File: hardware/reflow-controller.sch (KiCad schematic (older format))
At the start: 20 parts, among them J1 USB_B_Mini, J2 Conn_01x02, J3 Conn_02x03_Odd_Even, J4 Conn_01x02, J5 Conn_01x04, Q1 BC817, U1 MAX31855KASA, U2 AP2127K-3.3, U3 ATMEGA8U2-AU, Y1 8MHz

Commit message: PCB passes DRC.
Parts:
- removed J1: USB_B_Mini, symbol Connector_Specialized:USB_B_Mini
- removed U3: ATMEGA8U2-AU, TQFP-32, symbol MCU_Atmel_ATMEGA:ATMEGA8U2-AU
- added C7, C8: 0.1u, Capacitor_SMD:C_0603_1608Metric, symbol Device:C
- added C9: 10n, Capacitor_SMD:C_0603_1608Metric, symbol Device:C
- added D2: LED, LED_SMD:LED_0603_1608Metric, symbol Device:LED
- added J1: USB_B_Mini, Connector_USB:USB_Mini-B_Lumberg_2486_01_Horizontal, symbol Connector:USB_B_Mini
- added R4: 240, Resistor_SMD:R_0603_1608Metric, symbol Device:R
- added R5: 10k, Resistor_SMD:R_0603_1608Metric, symbol Device:R
- added R6: 1k, Resistor_SMD:R_0603_1608Metric, symbol Device:R
- added U3: ATmega8U2-AU, Package_QFP:TQFP-32_7x7mm_P0.8mm, symbol MCU_Microchip_ATmega:ATmega8U2-AU
- C1, C2, C3, C4, C5, C6: footprint (none) -> Capacitor_SMD:C_0603_1608Metric
- D1: footprint (none) -> Diode_SMD:D_SOD-323
- J2: footprint (none) -> TerminalBlock_Phoenix:TerminalBlock_Phoenix_MKDS-1,5-2_1x02_P5.00mm_Horizontal
- J3: footprint (none) -> Connector_PinHeader_2.54mm:PinHeader_2x03_P2.54mm_Vertical
- J4: footprint (none) -> Connector_PinHeader_2.54mm:PinHeader_1x02_P2.54mm_Vertical
- J5: footprint (none) -> Connector_PinHeader_2.54mm:PinHeader_1x04_P2.54mm_Vertical
- R1, R2: footprint (none) -> Resistor_SMD:R_0603_1608Metric
- R3: value 4.7k -> 10k; footprint (none) -> Resistor_SMD:R_0603_1608Metric
- Y1: footprint (none) -> Crystal:Crystal_SMD_HC49-SD
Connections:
- wire segments 78 -> 100
- no-connect marks 16 -> 15
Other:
- moved on the sheet: C1, C4, C5, C6, D1, J2, J4, Q1, R1, R2, R3, Y1

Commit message: Fixed power supply when programmed by ISP, added mounting holes, replaced mini USB connector with micro connector.
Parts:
- removed J1: USB_B_Mini, Connector_USB:USB_Mini-B_Lumberg_2486_01_Horizontal, symbol Connector:USB_B_Mini
- added J1: USB_B_Micro, Connector_USB:USB_Micro-B_Amphenol_10103594-0001LF_Horizontal, symbol Connector:USB_B_Micro
- added MH1, MH2, MH3, MH4: MountingHole_Pad, MountingHole:MountingHole_2.7mm_M2.5_Pad_Via, symbol Mechanical:MountingHole_Pad
- U3: symbol MCU_Microchip_ATmega:ATmega8U2-AU -> reflow-controller-rescue:ATmega8U2-AU-MCU_Microchip_ATmega
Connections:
- wire segments 100 -> 104
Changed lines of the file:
@@
 	7950 1550 8300 1550
 Text Label 8300 1550 2    50   ~ 0
-VCC
+VBUS
 Wire Wire Line
 	7950 1650 8300 1650
@@
 	5500 3800 5500 3950
 $Comp
-L MCU_Microchip_ATmega:ATmega8U2-AU U3
+L reflow-controller-rescue:ATmega8U2-AU-MCU_Microchip_ATmega U3
 U 1 1 5B3659A5
 P 7400 4400
@@
 Wire Wire Line
 	7300 2700 7300 2400
-$Comp
-L Connector:USB_B_Mini J1
-U 1 1 5B3FB3D2
-P 2500 4350
-F 0 "J1" H 2555 4817 50  0000 C CNN
-F 1 "USB_B_Mini" H 2555 4726 50  0000 C CNN
-F 2 "Connector_USB:USB_Mini-B_Lumberg_2486_01_Horizontal" H 2650 4300 50  0001 C CNN
-F 3 "~" H 2650 4300 50  0001 C CNN
-	1    2500 4350
-	1    0    0    -1
-$EndComp
 NoConn ~ 2800 4550
 Wire Wire Line
@@
 Wire Wire Line
 	2550 1700 2550 1800
+$Comp
+L Connector:USB_B_Micro J1
+U 1 1 5BB4219C
+P 2500 4350
+F 0 "J1" H 2555 4817 50  0000 C CNN
+F 1 "USB_B_Micro" H 2555 4726 50  0000 C CNN
+F 2 "Connector_USB:USB_Micro-B_Amphenol_10103594-0001LF_Horizontal" H 2650 4300 50  0001 C CNN
+F 3 "~" H 2650 4300 50  0001 C CNN
+	1    2500 4350
+	1    0    0    -1
+$EndComp
+$Comp
+L Mechanical:MountingHole_Pad MH2
+U 1 1 5BB44E9C
+P 1600 1250
+F 0 "MH2" H 1700 1301 50  0000 L CNN
+F 1 "MountingHole_Pad" H 1700 1210 50  0000 L CNN
+F 2 "MountingHole:MountingHole_2.7mm_M2.5_Pad_Via" H 1600 1250 50  0001 C CNN
+F 3 "~" H 1600 1250 50  0001 C CNN
+	1    1600 1250
+	1    0    0    -1
+$EndComp
+$Comp
+L Mechanical:MountingHole_Pad MH3
+U 1 1 5BB44F1A
+P 10600 1100
+F 0 "MH3" H 10700 1151 50  0000 L CNN
+F 1 "MountingHole_Pad" H 10700 1060 50  0000 L CNN
+F 2 "MountingHole:MountingHole_2.7mm_M2.5_Pad_Via" H 10600 1100 50  0001 C CNN
+F 3 "~" H 10600 1100 50  0001 C CNN
+	1    10600 1100
+	1    0    0    -1
+$EndComp
+$Comp
+L Mechanical:MountingHole_Pad MH4
+U 1 1 5BB44F98
+P 10600 6050
+F 0 "MH4" H 10700 6101 50  0000 L CNN
+F 1 "MountingHole_Pad" H 10700 6010 50  0000 L CNN
+F 2 "MountingHole:MountingHole_2.7mm_M2.5_Pad_Via" H 10600 6050 50  0001 C CNN
+F 3 "~" H 10600 6050 50  0001 C CNN
+	1    10600 6050
+	1    0    0    -1
+$EndComp
+$Comp
+L Mechanical:MountingHole_Pad MH1
+U 1 1 5BB4500A
+P 1500 6150
+F 0 "MH1" H 1600 6201 50  0000 L CNN
+F 1 "MountingHole_Pad" H 1600 6110 50  0000 L CNN
+F 2 "MountingHole:MountingHole_2.7mm_M2.5_Pad_Via" H 1500 6150 50  0001 C CNN
+F 3 "~" H 1500 6150 50  0001 C CNN
+	1    1500 6150
+	1    0    0    -1
+$EndComp
+$Comp
+L power:GND #PWR0101
+U 1 1 5BB451EE
+P 1600 1500
+F 0 "#PWR0101" H 1600 1250 50  0001 C CNN
+F 1 "GND" H 1605 1327 50  0000 C CNN
+F 2 "" H 1600 1500 50  0001 C CNN
+F 3 "" H 1600 1500 50  0001 C CNN
+	1    1600 1500
+	1    0    0    -1
+$EndComp
+$Comp
+L power:GND #PWR0102
+U 1 1 5BB45237
+P 1500 6400
+F 0 "#PWR0102" H 1500 6150 50  0001 C CNN
+F 1 "GND" H 1505 6227 50  0000 C CNN
+F 2 "" H 1500 6400 50  0001 C CNN
+F 3 "" H 1500 6400 50  0001 C CNN
+	1    1500 6400
+	1    0    0    -1
+$EndComp
+$Comp
+L power:GND #PWR0113
+U 1 1 5BB45280
+P 10600 6300
+F 0 "#PWR0113" H 10600 6050 50  0001 C CNN
+F 1 "GND" H 10605 6127 50  0000 C CNN
+F 2 "" H 10600 6300 50  0001 C CNN
+F 3 "" H 10600 6300 50  0001 C CNN
+	1    10600 6300
+	1    0    0    -1
+$EndComp
+$Comp
+L power:GND #PWR0114
+U 1 1 5BB4FB0F
+P 10600 1350
+F 0 "#PWR0114" H 10600 1100 50  0001 C CNN
+F 1 "GND" H 10605 1177 50  0000 C CNN
+F 2 "" H 10600 1350 50  0001 C CNN
+F 3 "" H 10600 1350 50  0001 C CNN
+	1    10600 1350
+	1    0    0    -1
+$EndComp
+Wire Wire Line
+	10600 1350 10600 1200
+Wire Wire Line
+	10600 6150 10600 6300
+Wire Wire Line
+	1500 6250 1500 6400
+Wire Wire Line
+	1600 1500 1600 1350
 $EndSCHEMATC

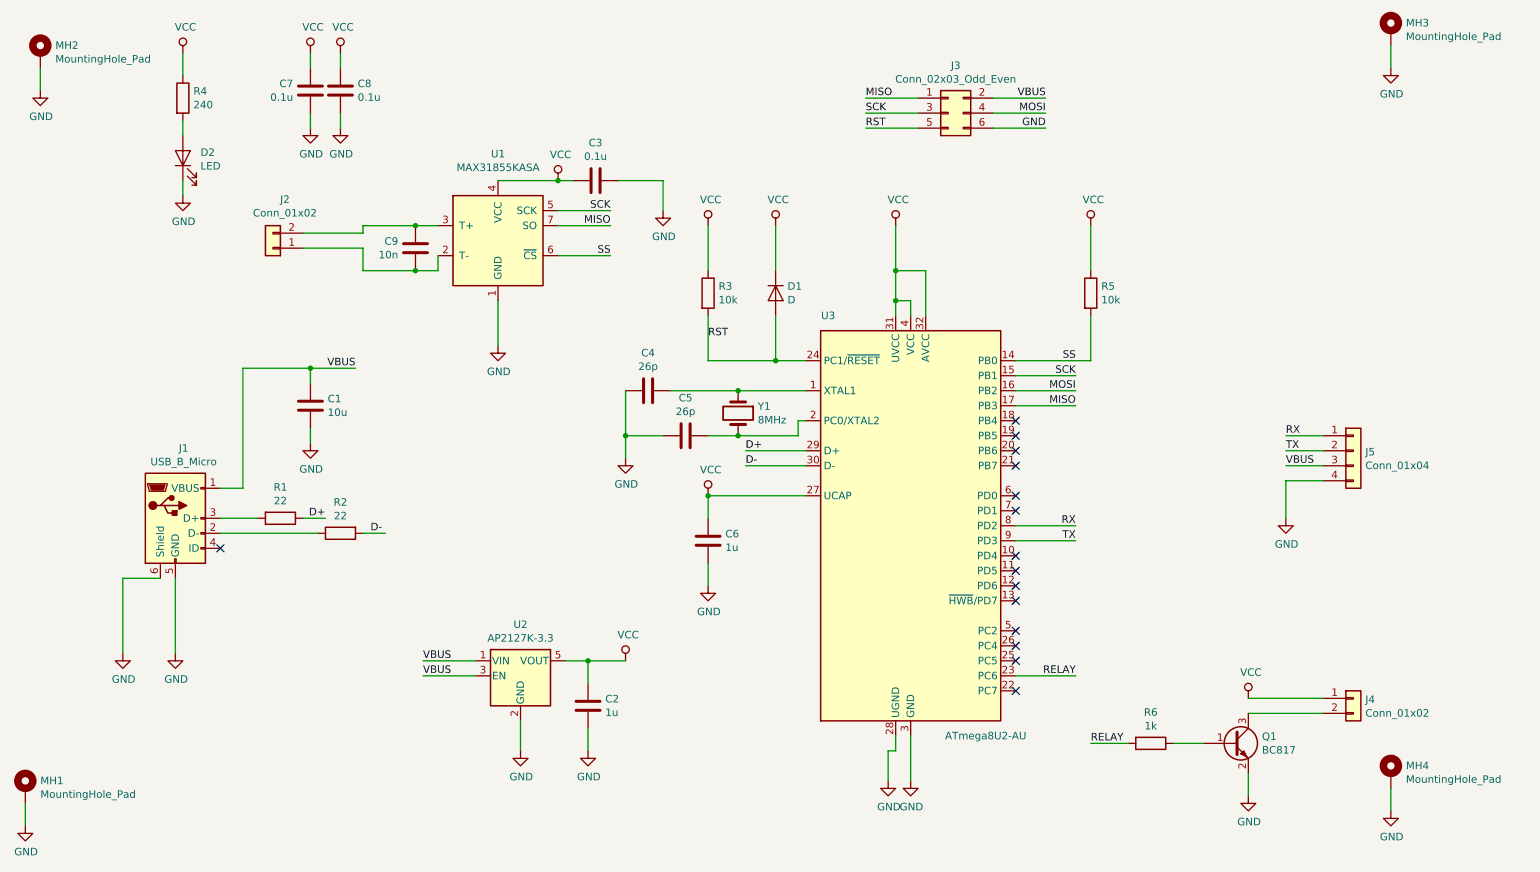
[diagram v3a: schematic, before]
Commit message: Bom generation improvements.
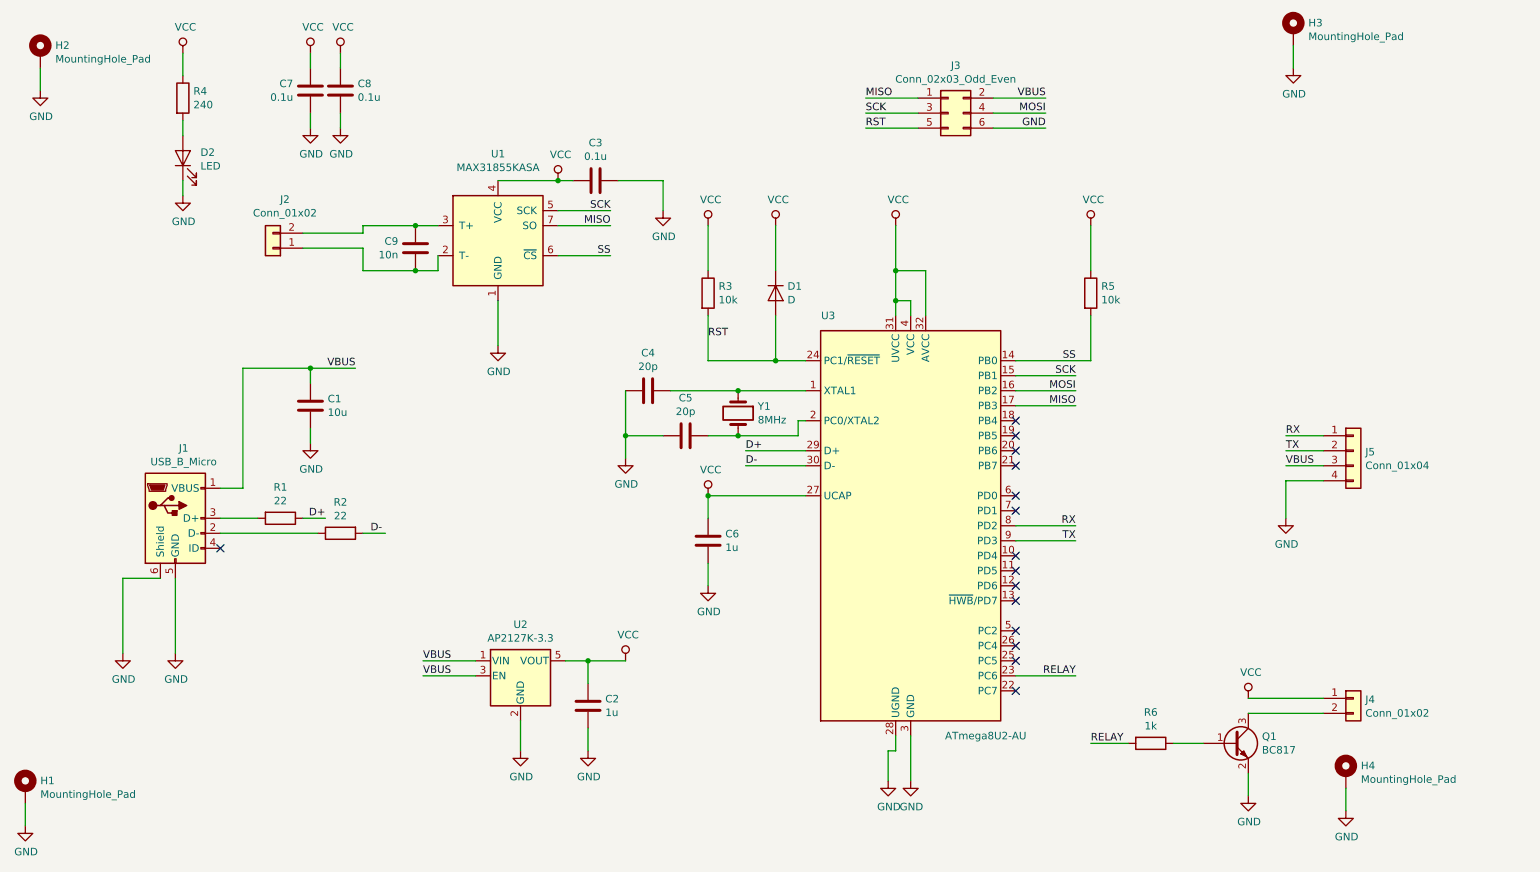
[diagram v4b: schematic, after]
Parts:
- C1: MFN (none) -> CL10A106KP8NNNC
- C2, C6: MFN (none) -> GRM188R60J105KA01D
- C3, C7, C8: MFN (none) -> CL10B104KO8NNNC
- C4, C5: value 26p -> 20p; MFN (none) -> CL10C200JB8NNNC
- C9: MFN (none) -> C1608X7R2A103M080AA
- D1: MFN (none) -> 1N4148WS-7-F
- D2: MFN (none) -> SML-D12V8WT86
- J2: MFN (none) -> 1935161
- Q1: MFN (none) -> BC817-40Q-13-F; manf# BC817-40Q-13-F -> (none)
- R1, R2: MFN (none) -> CR0603-JW-220ELF; Tolerance 5% -> (none)
- R3, R5: MFN (none) -> CR0603-FX-1002HLF
- R4: MFN (none) -> ERA-3AEB241V
- R6: MFN (none) -> CR0603-FX-1001HLF
- U1: MFN (none) -> MAX31855KASA+T; manf# MAX31855KASA+T -> (none)
- U2: MFN (none) -> AP2127K-3.3TRG1; manf# AP2127K-3.3TRG1 -> (none)
- U3: MFN (none) -> ATMEGA8U2-AU
- Y1: MFN (none) -> ABLS-8.000MHZ-B4-T; manf# ABLS-8.000MHZ-B4-T -> (none)
- renumbered MH1 to H1, MH2 to H2, MH3 to H3, MH4 to H4
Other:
- moved on the sheet: H3, H4
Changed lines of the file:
@@
 EESchema Schematic File Version 4
 LIBS:reflow-controller-cache
-EELAYER 29 0
+EELAYER 26 0
 EELAYER END
 $Descr A4 11693 8268
@@
 F 2 "Resistor_SMD:R_0603_1608Metric" V 3130 4350 50  0001 C CNN
 F 3 "~" H 3200 4350 50  0001 C CNN
-F 4 "5%" V 3200 4350 50  0001 C CNN "Tolerance"
+F 4 "CR0603-JW-220ELF" V 3200 4350 50  0001 C CNN "MFN"
 	1    3200 4350
 	0    1    1    0
@@
 F 2 "Resistor_SMD:R_0603_1608Metric" V 3530 4450 50  0001 C CNN
 F 3 "~" H 3600 4450 50  0001 C CNN
-F 4 "5%" V 3600 4450 50  0001 C CNN "Tolerance"
+F 4 "CR0603-JW-220ELF" V 3600 4450 50  0001 C CNN "MFN"
 	1    3600 4450
 	0    -1   1    0
@@
 F 2 "Capacitor_SMD:C_0603_1608Metric" H 6088 4350 50  0001 C CNN
 F 3 "~" H 6050 4500 50  0001 C CNN
+F 4 "GRM188R60J105KA01D" H 6050 4500 50  0001 C CNN "MFN"
 	1    6050 4500
 	1    0    0    -1
@@
 F 2 "Crystal:Crystal_SMD_HC49-SD" H 6250 3650 50  0001 C CNN
 F 3 "~" H 6250 3650 50  0001 C CNN
-F 4 "ABLS-8.000MHZ-B4-T" V 6250 3650 50  0001 C CNN "manf#"
+F 4 "ABLS-8.000MHZ-B4-T" V 6250 3650 50  0001 C CNN "MFN"
 	1    6250 3650
 	0    1    1    0
@@
 P 5650 3500
 F 0 "C4" V 5398 3500 50  0000 C CNN
-F 1 "26p" V 5489 3500 50  0000 C CNN
+F 1 "20p" V 5489 3500 50  0000 C CNN
 F 2 "Capacitor_SMD:C_0603_1608Metric" H 5688 3350 50  0001 C CNN
 F 3 "~" H 5650 3500 50  0001 C CNN
+F 4 "CL10C200JB8NNNC" V 5650 3500 50  0001 C CNN "MFN"
 	1    5650 3500
 	0    1    1    0
@@
 P 5900 3800
 F 0 "C5" V 5648 3800 50  0000 C CNN
-F 1 "26p" V 5739 3800 50  0000 C CNN
+F 1 "20p" V 5739 3800 50  0000 C CNN
 F 2 "Capacitor_SMD:C_0603_1608Metric" H 5938 3650 50  0001 C CNN
 F 3 "~" H 5900 3800 50  0001 C CNN
+F 4 "CL10C200JB8NNNC" V 5900 3800 50  0001 C CNN "MFN"
 	1    5900 3800
 	0    1    1    0
@@
 F 2 "Package_SO:SOIC-8_3.9x4.9mm_P1.27mm" H 5650 2150 50  0001 C CIN
 F 3 "http://datasheets.maximintegrated.com/en/ds/MAX31855.pdf" H 4650 2500 50  0001 C CNN
-F 4 "MAX31855KASA+T" H 4650 2500 50  0001 C CNN "manf#"
+F 4 "MAX31855KASA+T" H 4650 2500 50  0001 C CNN "MFN"
 	1    4650 2500
 	1    0    0    -1
@@
 F 2 "Capacitor_SMD:C_0603_1608Metric" H 5338 1950 50  0001 C CNN
 F 3 "~" H 5300 2100 50  0001 C CNN
+F 4 "CL10B104KO8NNNC" V 5300 2100 50  0001 C CNN "MFN"
 	1    5300 2100
 	0    1    1    0
@@
 F 2 "TerminalBlock_Phoenix:TerminalBlock_Phoenix_MKDS-1,5-2_1x02_P5.00mm_Horizontal" H 3150 2550 50  0001 C CNN
 F 3 "~" H 3150 2550 50  0001 C CNN
+F 4 "1935161" H 3150 2550 50  0001 C CNN "MFN"
 	1    3150 2550
 	-1   0    0    1
@@
 F 2 "Resistor_SMD:R_0603_1608Metric" V 5980 2850 50  0001 C CNN
 F 3 "~" H 6050 2850 50  0001 C CNN
+F 4 "CR0603-FX-1002HLF" H 6050 2850 50  0001 C CNN "MFN"
 	1    6050 2850
 	1    0    0    -1
@@
 F 2 "Diode_SMD:D_SOD-323" H 6500 2850 50  0001 C CNN
 F 3 "~" H 6500 2850 50  0001 C CNN
+F 4 "1N4148WS-7-F" V 6500 2850 50  0001 C CNN "MFN"
 	1    6500 2850
 	0    1    1    0
@@
 F 2 "Package_TO_SOT_SMD:SOT-23-5" H 4800 5725 50  0001 C CNN
 F 3 "https://www.diodes.com/assets/Datasheets/AP2127.pdf" H 4800 5500 50  0001 C CNN
-F 4 "AP2127K-3.3TRG1" H 4800 5400 50  0001 C CNN "manf#"
+F 4 "AP2127K-3.3TRG1" H 4800 5400 50  0001 C CNN "MFN"
 	1    4800 5400
 	1    0    0    -1
@@
 F 2 "Capacitor_SMD:C_0603_1608Metric" H 3438 3450 50  0001 C CNN
 F 3 "~" H 3400 3600 50  0001 C CNN
+F 4 "CL10A106KP8NNNC" H 3400 3600 50  0001 C CNN "MFN"
 	1    3400 3600
 	1    0    0    -1
@@
 F 2 "Capacitor_SMD:C_0603_1608Metric" H 5288 5450 50  0001 C CNN
 F 3 "~" H 5250 5600 50  0001 C CNN
+F 4 "GRM188R60J105KA01D" H 5250 5600 50  0001 C CNN "MFN"
 	1    5250 5600
 	1    0    0    -1
@@
 F 2 "Package_TO_SOT_SMD:SOT-23" H 9750 5775 50  0001 L CIN
 F 3 "http://www.fairchildsemi.com/ds/BC/BC817.pdf" H 9550 5850 50  0001 L CNN
-F 4 "BC817-40Q-13-F" H 9550 5850 50  0001 C CNN "manf#"
+F 4 "BC817-40Q-13-F" H 9550 5850 50  0001 C CNN "MFN"
 	1    9550 5850
 	1    0    0    -1
@@
 F 2 "Capacitor_SMD:C_0603_1608Metric" H 3438 1350 50  0001 C CNN
 F 3 "~" H 3400 1500 50  0001 C CNN
+F 4 "CL10B104KO8NNNC" H 3400 1500 50  0001 C CNN "MFN"
 	1    3400 1500
 	1    0    0    -1
@@
 F 2 "Capacitor_SMD:C_0603_1608Metric" H 3638 1350 50  0001 C CNN
 F 3 "~" H 3600 1500 50  0001 C CNN
+F 4 "CL10B104KO8NNNC" H 3600 1500 50  0001 C CNN "MFN"
 	1    3600 1500
 	1    0    0    -1
@@
 F 2 "Package_QFP:TQFP-32_7x7mm_P0.8mm" H 7400 4400 50  0001 C CIN
 F 3 "http://ww1.microchip.com/downloads/en/DeviceDoc/doc7799.pdf" H 7400 4400 50  0001 C CNN
+F 4 "ATMEGA8U2-AU" H 7400 4400 50  0001 C CNN "MFN"
 	1    7400 4400
 	1    0    0    -1
@@
 F 2 "Resistor_SMD:R_0603_1608Metric" V 8930 5850 50  0001 C CNN
 F 3 "~" H 9000 5850 50  0001 C CNN
+F 4 "CR0603-FX-1001HLF" V 9000 5850 50  0001 C CNN "MFN"
 	1    9000 5850
 	0    1    1    0
@@
 F 2 "Capacitor_SMD:C_0603_1608Metric" H 4138 2400 50  0001 C CNN
 F 3 "~" H 4100 2550 50  0001 C CNN
+F 4 "C1608X7R2A103M080AA" H 4100 2550 50  0001 C CNN "MFN"
 	1    4100 2550
 	1    0    0    -1
@@
 F 2 "Resistor_SMD:R_0603_1608Metric" V 8530 2850 50  0001 C CNN
 F 3 "~" H 8600 2850 50  0001 C CNN
+F 4 "CR0603-FX-1002HLF" H 8600 2850 50  0001 C CNN "MFN"
 	1    8600 2850
 	1    0    0    -1
@@
 F 2 "LED_SMD:LED_0603_1608Metric" H 2550 1950 50  0001 C CNN
 F 3 "~" H 2550 1950 50  0001 C CNN
+F 4 "SML-D12V8WT86" V 2550 1950 50  0001 C CNN "MFN"
 	1    2550 1950
 	0    -1   -1   0
@@
 F 2 "Resistor_SMD:R_0603_1608Metric" V 2480 1550 50  0001 C CNN
 F 3 "~" H 2550 1550 50  0001 C CNN
+F 4 "ERA-3AEB241V" H 2550 1550 50  0001 C CNN "MFN"
 	1    2550 1550
 	1    0    0    -1
@@
 $EndComp
 $Comp
-L Mechanical:MountingHole_Pad MH2
+L Mechanical:MountingHole_Pad H2
 U 1 1 5BB44E9C
 P 1600 1250
-F 0 "MH2" H 1700 1301 50  0000 L CNN
+F 0 "H2" H 1700 1301 50  0000 L CNN
 F 1 "MountingHole_Pad" H 1700 1210 50  0000 L CNN
 F 2 "MountingHole:MountingHole_2.7mm_M2.5_Pad_Via" H 1600 1250 50  0001 C CNN
@@
 $EndComp
 $Comp
-L Mechanical:MountingHole_Pad MH3
+L Mechanical:MountingHole_Pad H3
 U 1 1 5BB44F1A
-P 10600 1100
-F 0 "MH3" H 10700 1151 50  0000 L CNN
-F 1 "MountingHole_Pad" H 10700 1060 50  0000 L CNN
-F 2 "MountingHole:MountingHole_2.7mm_M2.5_Pad_Via" H 10600 1100 50  0001 C CNN
-F 3 "~" H 10600 1100 50  0001 C CNN
-	1    10600 1100
-	1    0    0    -1
-$EndComp
-$Comp
-L Mechanical:MountingHole_Pad MH4
+P 9950 1100
+F 0 "H3" H 10050 1151 50  0000 L CNN
+F 1 "MountingHole_Pad" H 10050 1060 50  0000 L CNN
+F 2 "MountingHole:MountingHole_2.7mm_M2.5_Pad_Via" H 9950 1100 50  0001 C CNN
+F 3 "~" H 9950 1100 50  0001 C CNN
+	1    9950 1100
+	1    0    0    -1
+$EndComp
+$Comp
+L Mechanical:MountingHole_Pad H4
 U 1 1 5BB44F98
-P 10600 6050
-F 0 "MH4" H 10700 6101 50  0000 L CNN
-F 1 "MountingHole_Pad" H 10700 6010 50  0000 L CNN
-F 2 "MountingHole:MountingHole_2.7mm_M2.5_Pad_Via" H 10600 6050 50  0001 C CNN
-F 3 "~" H 10600 6050 50  0001 C CNN
-	1    10600 6050
-	1    0    0    -1
-$EndComp
-$Comp
-L Mechanical:MountingHole_Pad MH1
+P 10300 6050
+F 0 "H4" H 10400 6101 50  0000 L CNN
+F 1 "MountingHole_Pad" H 10400 6010 50  0000 L CNN
+F 2 "MountingHole:MountingHole_2.7mm_M2.5_Pad_Via" H 10300 6050 50  0001 C CNN
+F 3 "~" H 10300 6050 50  0001 C CNN
+	1    10300 6050
+	1    0    0    -1
+$EndComp
+$Comp
+L Mechanical:MountingHole_Pad H1
 U 1 1 5BB4500A
 P 1500 6150
-F 0 "MH1" H 1600 6201 50  0000 L CNN
+F 0 "H1" H 1600 6201 50  0000 L CNN
 F 1 "MountingHole_Pad" H 1600 6110 50  0000 L CNN
 F 2 "MountingHole:MountingHole_2.7mm_M2.5_Pad_Via" H 1500 6150 50  0001 C CNN
@@
 L power:GND #PWR0113
 U 1 1 5BB45280
-P 10600 6300
-F 0 "#PWR0113" H 10600 6050 50  0001 C CNN
-F 1 "GND" H 10605 6127 50  0000 C CNN
-F 2 "" H 10600 6300 50  0001 C CNN
-F 3 "" H 10600 6300 50  0001 C CNN
-	1    10600 6300
+P 10300 6300
+F 0 "#PWR0113" H 10300 6050 50  0001 C CNN
+F 1 "GND" H 10305 6127 50  0000 C CNN
+F 2 "" H 10300 6300 50  0001 C CNN
+F 3 "" H 10300 6300 50  0001 C CNN
+	1    10300 6300
 	1    0    0    -1
 $EndComp
@@
 L power:GND #PWR0114
 U 1 1 5BB4FB0F
-P 10600 1350
-F 0 "#PWR0114" H 10600 1100 50  0001 C CNN
-F 1 "GND" H 10605 1177 50  0000 C CNN
-F 2 "" H 10600 1350 50  0001 C CNN
-F 3 "" H 10600 1350 50  0001 C CNN
-	1    10600 1350
-	1    0    0    -1
-$EndComp
-Wire Wire Line
-	10600 1350 10600 1200
-Wire Wire Line
-	10600 6150 10600 6300
+P 9950 1350
+F 0 "#PWR0114" H 9950 1100 50  0001 C CNN
+F 1 "GND" H 9955 1177 50  0000 C CNN
+F 2 "" H 9950 1350 50  0001 C CNN
+F 3 "" H 9950 1350 50  0001 C CNN
+	1    9950 1350
+	1    0    0    -1
+$EndComp
+Wire Wire Line
+	9950 1350 9950 1200
+Wire Wire Line
+	10300 6150 10300 6300
 Wire Wire Line
 	1500 6250 1500 6400

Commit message: Improved pc software and added MFN to schematic for USB receptacle.
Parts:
- J1: MFN (none) -> 10103594-0001LF
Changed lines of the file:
@@
 F 2 "Connector_USB:USB_Micro-B_Amphenol_10103594-0001LF_Horizontal" H 2650 4300 50  0001 C CNN
 F 3 "~" H 2650 4300 50  0001 C CNN
+F 4 "10103594-0001LF" H 2500 4350 50  0001 C CNN "MFN"
 	1    2500 4350
 	1    0    0    -1
